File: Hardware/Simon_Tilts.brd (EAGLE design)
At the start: 76.2 x 68.6 mm, 44 parts

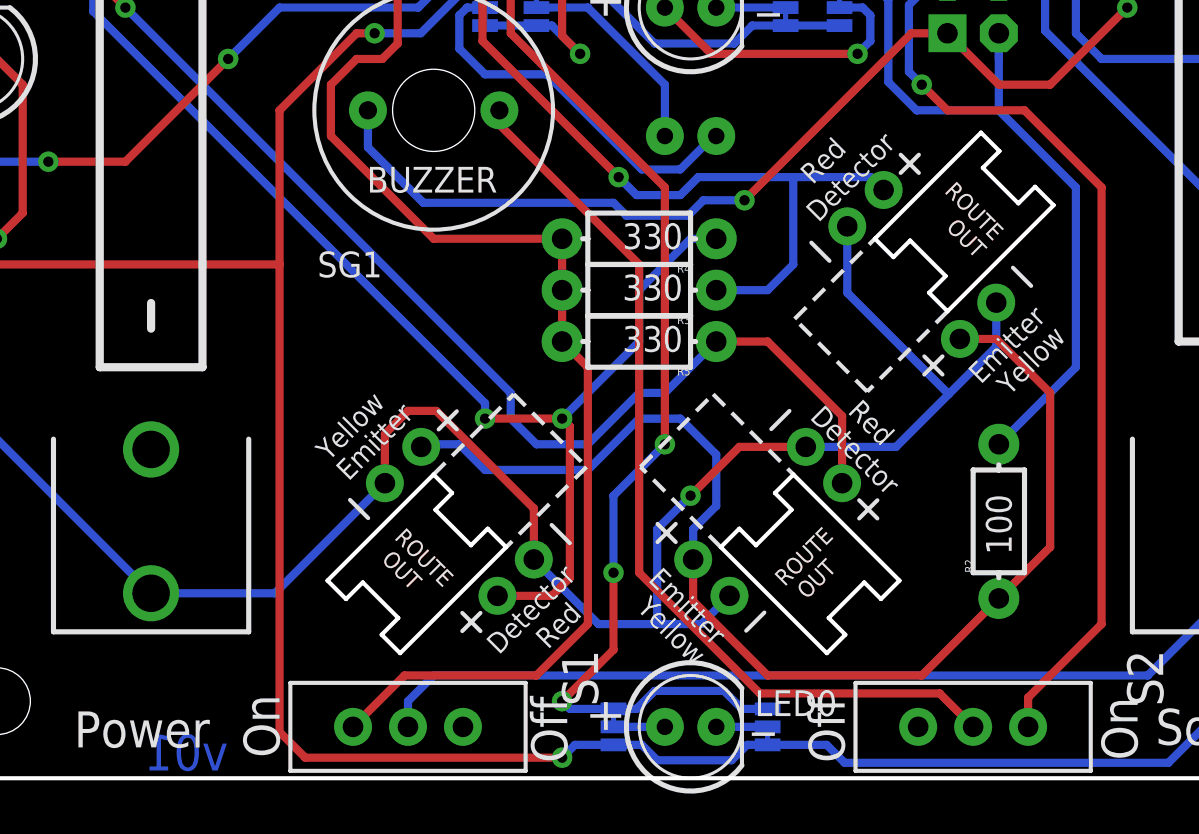
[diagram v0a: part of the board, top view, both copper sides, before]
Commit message: V10 ready for red boards
-Updated tilt sensor package to TILT_SENSOR_V5, then rerouted irregular
traces.
-Changed version to "V10" in bottom copper AND schematic.
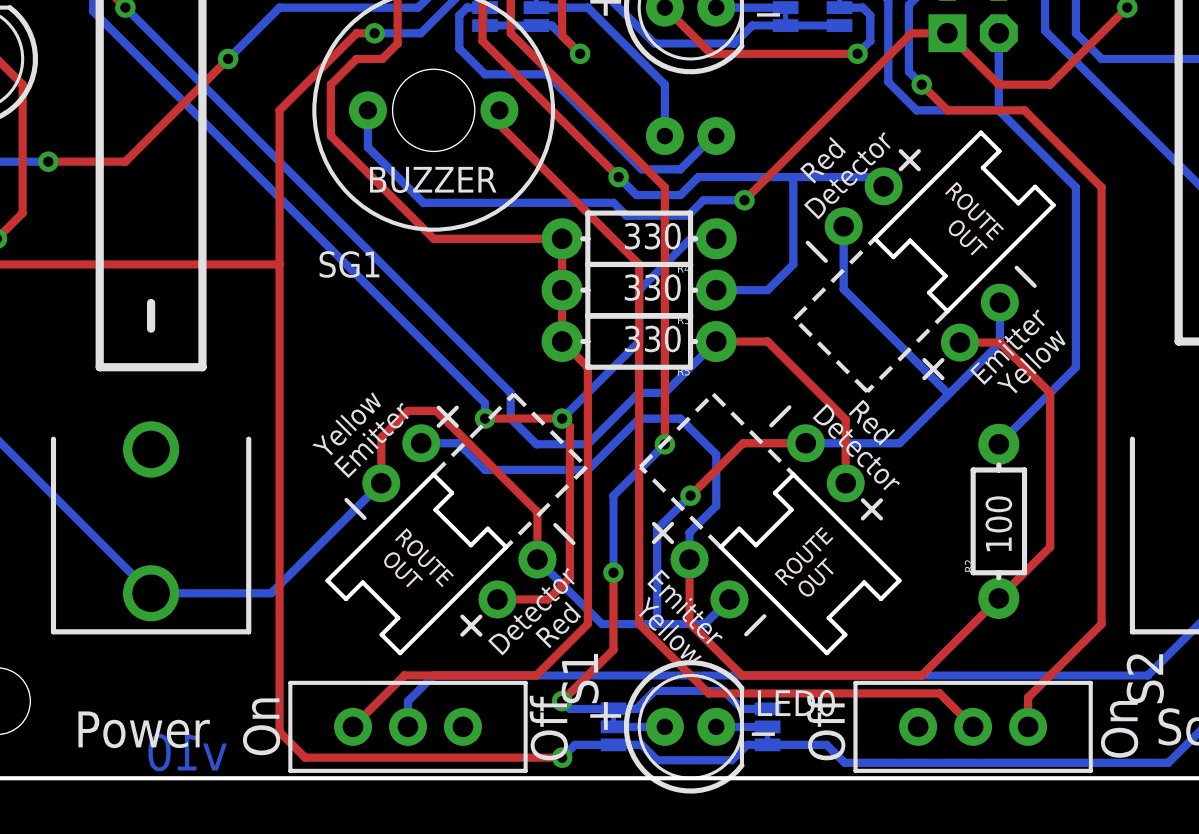
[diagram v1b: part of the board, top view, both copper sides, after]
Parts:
- U$4, U$5, U$6: value TILT_SENSORV4 -> TILT_SENSORV5; device Testing:TILT_SENSOR_V4 -> Testing:TILT_SENSOR_V5
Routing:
- net N$3: track 45.4 -> 46.9 mm
- net N$6: track 59.7 -> 60.4 mm
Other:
- board text added: "v10"
- board text removed: "v01"
